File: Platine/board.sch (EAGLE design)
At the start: 10 parts, among them T1 BC847, T2 BC847

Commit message: Update PCB
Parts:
- removed C1, C2: 100µ, resistor:C-EUC0805
- added C4, C5: 100µ, resistor:CPOL-EU153CLV-0605
- added J1: (no value), con-jack:JACK-PLUG1
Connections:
- net +5V: now also J1.3
- net GND: now also J1.1, J1.2
- net N$6: now also C4.-; no longer C1.2
- net N$7: now also C5.-; no longer C2.1
- net N$8: now also C4.+; no longer C1.1
- net N$9: now also C5.+; no longer C2.2
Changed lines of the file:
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@@
 <part name="LED1" library="led" library_urn="urn:adsk.eagle:library:259" deviceset="LED" device="CHIPLED_0805" package3d_urn="urn:adsk.eagle:package:15821/2" value="grün"/>
 <part name="R1" library="resistor" library_urn="urn:adsk.eagle:library:348" deviceset="R-EU_" device="R0805" package3d_urn="urn:adsk.eagle:package:23553/2" value="470"/>
-<part name="C1" library="resistor" library_urn="urn:adsk.eagle:library:348" deviceset="C-EU" device="C0805" package3d_urn="urn:adsk.eagle:package:23617/2" value="100µ"/>
 <part name="LED2" library="led" library_urn="urn:adsk.eagle:library:259" deviceset="LED" device="CHIPLED_0805" package3d_urn="urn:adsk.eagle:package:15821/2" value="grün"/>
 <part name="R2" library="resistor" library_urn="urn:adsk.eagle:library:348" deviceset="R-EU_" device="R0805" package3d_urn="urn:adsk.eagle:package:23553/2" value="470"/>
 <part name="R3" library="resistor" library_urn="urn:adsk.eagle:library:348" deviceset="R-EU_" device="R0805" package3d_urn="urn:adsk.eagle:package:23553/2" value="470"/>
 <part name="R4" library="resistor" library_urn="urn:adsk.eagle:library:348" deviceset="R-EU_" device="R0805" package3d_urn="urn:adsk.eagle:package:23553/2" value="470"/>
-<part name="C2" library="resistor" library_urn="urn:adsk.eagle:library:348" deviceset="C-EU" device="C0805" package3d_urn="urn:adsk.eagle:package:23617/2" value="100µ"/>
 <part name="T1" library="transistor" library_urn="urn:adsk.eagle:library:402" deviceset="BC847" device="" package3d_urn="urn:adsk.eagle:package:28738/2"/>
 <part name="T2" library="transistor" library_urn="urn:adsk.eagle:library:402" deviceset="BC847" device="" package3d_urn="urn:adsk.eagle:package:28738/2"/>
 <part name="P+1" library="supply1" library_urn="urn:adsk.eagle:library:371" deviceset="+5V" device=""/>
 <part name="GND1" library="supply1" library_urn="urn:adsk.eagle:library:371" deviceset="GND" device=""/>
+<part name="J1" library="con-jack" library_urn="urn:adsk.eagle:library:154" deviceset="JACK-PLUG" device="1" package3d_urn="urn:adsk.eagle:package:7494/1"/>
+<part name="P+2" library="supply1" library_urn="urn:adsk.eagle:library:371" deviceset="+5V" device=""/>
+<part name="GND2" library="supply1" library_urn="urn:adsk.eagle:library:371" deviceset="GND" device=""/>
+<part name="C4" library="resistor" library_urn="urn:adsk.eagle:library:348" deviceset="CPOL-EU" device="153CLV-0605" package3d_urn="urn:adsk.eagle:package:23398/2" value="100µ"/>
+<part name="C5" library="resistor" library_urn="urn:adsk.eagle:library:348" deviceset="CPOL-EU" device="153CLV-0605" package3d_urn="urn:adsk.eagle:package:23398/2" value="100µ"/>
 </parts>
 <sheets>
@@
 <attribute name="NAME" x="13.7414" y="46.99" size="1.778" layer="95" rot="R90"/>
 <attribute name="VALUE" x="18.542" y="46.99" size="1.778" layer="96" rot="R90"/>
-</instance>
-<instance part="C1" gate="G$1" x="35.56" y="45.72" smashed="yes" rot="R270">
-<attribute name="NAME" x="35.941" y="44.196" size="1.778" layer="95" rot="R270"/>
-<attribute name="VALUE" x="30.861" y="44.196" size="1.778" layer="96" rot="R270"/>
 </instance>
 <instance part="LED2" gate="G$1" x="15.24" y="63.5" smashed="yes">
@@
 <attribute name="VALUE" x="49.022" y="46.99" size="1.778" layer="96" rot="R90"/>
 </instance>
-<instance part="C2" gate="G$1" x="35.56" y="38.1" smashed="yes" rot="R270">
-<attribute name="NAME" x="35.941" y="36.576" size="1.778" layer="95" rot="R270"/>
-<attribute name="VALUE" x="30.861" y="36.576" size="1.778" layer="96" rot="R270"/>
-</instance>
 <instance part="T1" gate="G$1" x="17.78" y="33.02" smashed="yes" rot="MR0">
 <attribute name="NAME" x="27.94" y="40.64" size="1.778" layer="95" rot="MR0"/>
@@
 <instance part="GND1" gate="1" x="2.54" y="25.4" smashed="yes">
 <attribute name="VALUE" x="0" y="22.86" size="1.778" layer="96"/>
+</instance>
+<instance part="J1" gate="G$1" x="83.82" y="48.26" smashed="yes">
+<attribute name="NAME" x="76.2" y="53.34" size="1.778" layer="95"/>
+<attribute name="VALUE" x="76.2" y="43.18" size="1.778" layer="96"/>
+</instance>
+<instance part="P+2" gate="1" x="93.98" y="58.42" smashed="yes">
+<attribute name="VALUE" x="91.44" y="53.34" size="1.778" layer="96" rot="R90"/>
+</instance>
+<instance part="GND2" gate="1" x="93.98" y="43.18" smashed="yes">
+<attribute name="VALUE" x="91.44" y="40.64" size="1.778" layer="96"/>
+</instance>
+<instance part="C4" gate="G$1" x="35.56" y="45.72" smashed="yes" rot="R270">
+<attribute name="NAME" x="36.0426" y="44.577" size="1.778" layer="95" rot="R270"/>
+<attribute name="VALUE" x="30.9626" y="44.577" size="1.778" layer="96" rot="R270"/>
+</instance>
+<instance part="C5" gate="G$1" x="33.02" y="38.1" smashed="yes" rot="R90">
+<attribute name="NAME" x="32.5374" y="31.623" size="1.778" layer="95" rot="R90"/>
+<attribute name="VALUE" x="37.6174" y="31.623" size="1.778" layer="96" rot="R90"/>
 </instance>
 </instances>
@@
 <junction x="45.72" y="66.04"/>
 </segment>
+<segment>
+<pinref part="J1" gate="G$1" pin="3"/>
+<pinref part="P+2" gate="1" pin="+5V"/>
+<wire x1="88.9" y1="50.8" x2="93.98" y2="50.8" width="0.1524" layer="91"/>
+<wire x1="93.98" y1="50.8" x2="93.98" y2="55.88" width="0.1524" layer="91"/>
+</segment>
 </net>
 <net name="GND" class="0">
@@
 <wire x1="15.24" y1="27.94" x2="53.34" y2="27.94" width="0.1524" layer="91"/>
 </segment>
+<segment>
+<pinref part="J1" gate="G$1" pin="2"/>
+<pinref part="J1" gate="G$1" pin="1"/>
+<wire x1="88.9" y1="48.26" x2="88.9" y2="45.72" width="0.1524" layer="91"/>
+<pinref part="GND2" gate="1" pin="GND"/>
+<wire x1="88.9" y1="45.72" x2="93.98" y2="45.72" width="0.1524" layer="91"/>
+<junction x="88.9" y="45.72"/>
+</segment>
 </net>
 <net name="N$6" class="0">
@@
 <wire x1="15.24" y1="43.18" x2="15.24" y2="45.72" width="0.1524" layer="91"/>
 <wire x1="15.24" y1="43.18" x2="30.48" y2="43.18" width="0.1524" layer="91"/>
-<pinref part="C1" gate="G$1" pin="2"/>
 <wire x1="30.48" y1="43.18" x2="30.48" y2="45.72" width="0.1524" layer="91"/>
 <junction x="15.24" y="43.18"/>
+<pinref part="C4" gate="G$1" pin="-"/>
 </segment>
 </net>
@@
 <pinref part="T2" gate="G$1" pin="C"/>
 <wire x1="53.34" y1="45.72" x2="53.34" y2="38.1" width="0.1524" layer="91"/>
-<pinref part="C2" gate="G$1" pin="1"/>
 <wire x1="38.1" y1="38.1" x2="53.34" y2="38.1" width="0.1524" layer="91"/>
 <junction x="53.34" y="38.1"/>
+<pinref part="C5" gate="G$1" pin="-"/>
 </segment>
 </net>
 <net name="N$8" class="0">
 <segment>
-<pinref part="C1" gate="G$1" pin="1"/>
 <pinref part="R4" gate="G$1" pin="1"/>
 <wire x1="38.1" y1="45.72" x2="45.72" y2="45.72" width="0.1524" layer="91"/>
@@
 <wire x1="45.72" y1="33.02" x2="48.26" y2="33.02" width="0.1524" layer="91"/>
 <junction x="45.72" y="45.72"/>
+<pinref part="C4" gate="G$1" pin="+"/>
 </segment>
 </net>
@@
 <wire x1="22.86" y1="38.1" x2="22.86" y2="33.02" width="0.1524" layer="91"/>
 <wire x1="22.86" y1="33.02" x2="20.32" y2="33.02" width="0.1524" layer="91"/>
-<pinref part="C2" gate="G$1" pin="2"/>
 <wire x1="22.86" y1="38.1" x2="30.48" y2="38.1" width="0.1524" layer="91"/>
 <junction x="22.86" y="38.1"/>
+<pinref part="C5" gate="G$1" pin="+"/>
 </segment>
 </net>

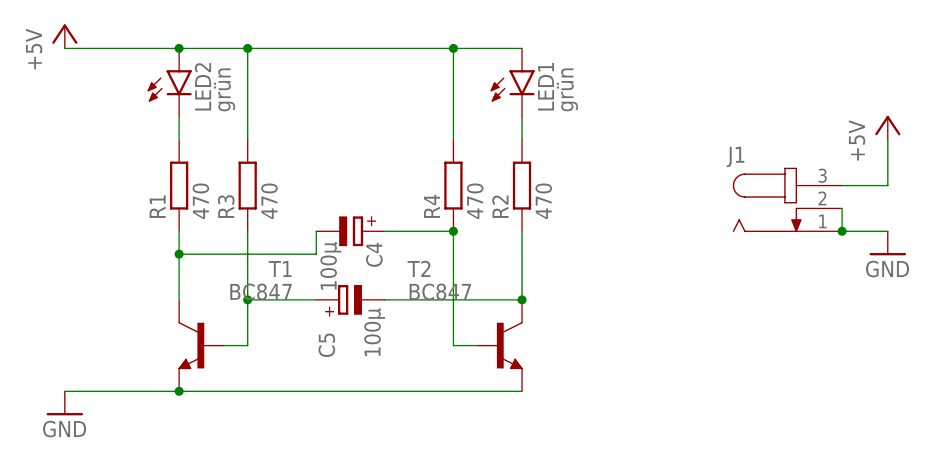
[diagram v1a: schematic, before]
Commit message: Update Platine: SMD Hohlstecker + Wire vergessen
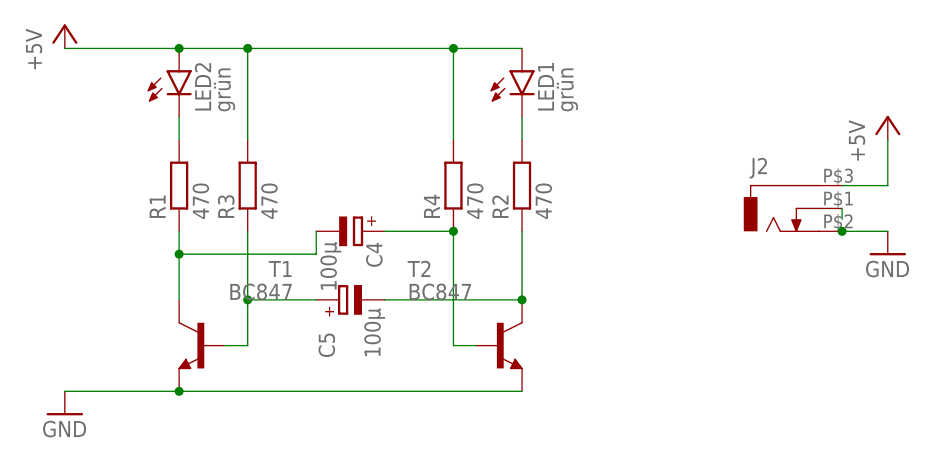
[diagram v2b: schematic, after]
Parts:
- removed J1: (no value), con-jack:JACK-PLUG1
- added J2: (no value), Hohlstecker-SMD:RASM7X2
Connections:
- new net N$19: J2.2
- net +5V: now also J2.1; no longer J1.3
- net GND: now also J2.3; no longer J1.1, J1.2
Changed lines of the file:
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@@
 <part name="P+1" library="supply1" library_urn="urn:adsk.eagle:library:371" deviceset="+5V" device=""/>
 <part name="GND1" library="supply1" library_urn="urn:adsk.eagle:library:371" deviceset="GND" device=""/>
-<part name="J1" library="con-jack" library_urn="urn:adsk.eagle:library:154" deviceset="JACK-PLUG" device="1" package3d_urn="urn:adsk.eagle:package:7494/1"/>
 <part name="P+2" library="supply1" library_urn="urn:adsk.eagle:library:371" deviceset="+5V" device=""/>
 <part name="GND2" library="supply1" library_urn="urn:adsk.eagle:library:371" deviceset="GND" device=""/>
 <part name="C4" library="resistor" library_urn="urn:adsk.eagle:library:348" deviceset="CPOL-EU" device="153CLV-0605" package3d_urn="urn:adsk.eagle:package:23398/2" value="100µ"/>
 <part name="C5" library="resistor" library_urn="urn:adsk.eagle:library:348" deviceset="CPOL-EU" device="153CLV-0605" package3d_urn="urn:adsk.eagle:package:23398/2" value="100µ"/>
+<part name="J2" library="Hohlstecker-SMD" deviceset="RASM7X2" device=""/>
 </parts>
 <sheets>
@@
 <attribute name="VALUE" x="0" y="22.86" size="1.778" layer="96"/>
 </instance>
-<instance part="J1" gate="G$1" x="83.82" y="48.26" smashed="yes">
-<attribute name="NAME" x="76.2" y="53.34" size="1.778" layer="95"/>
-<attribute name="VALUE" x="76.2" y="43.18" size="1.778" layer="96"/>
-</instance>
 <instance part="P+2" gate="1" x="93.98" y="58.42" smashed="yes">
 <attribute name="VALUE" x="91.44" y="53.34" size="1.778" layer="96" rot="R90"/>
@@
 <attribute name="NAME" x="32.5374" y="31.623" size="1.778" layer="95" rot="R90"/>
 <attribute name="VALUE" x="37.6174" y="31.623" size="1.778" layer="96" rot="R90"/>
+</instance>
+<instance part="J2" gate="G$1" x="81.28" y="48.26" smashed="yes">
+<attribute name="NAME" x="78.74" y="52.07" size="1.778" layer="95"/>
+<attribute name="VALUE" x="78.74" y="41.91" size="1.778" layer="96"/>
 </instance>
 </instances>
@@
 </segment>
 <segment>
-<pinref part="J1" gate="G$1" pin="3"/>
 <pinref part="P+2" gate="1" pin="+5V"/>
 <wire x1="88.9" y1="50.8" x2="93.98" y2="50.8" width="0.1524" layer="91"/>
 <wire x1="93.98" y1="50.8" x2="93.98" y2="55.88" width="0.1524" layer="91"/>
+<pinref part="J2" gate="G$1" pin="1"/>
 </segment>
 </net>
@@
 </segment>
 <segment>
-<pinref part="J1" gate="G$1" pin="2"/>
-<pinref part="J1" gate="G$1" pin="1"/>
-<wire x1="88.9" y1="48.26" x2="88.9" y2="45.72" width="0.1524" layer="91"/>
 <pinref part="GND2" gate="1" pin="GND"/>
 <wire x1="88.9" y1="45.72" x2="93.98" y2="45.72" width="0.1524" layer="91"/>
+<wire x1="88.9" y1="45.72" x2="88.9" y2="45.72" width="0.1524" layer="91"/>
+<pinref part="J2" gate="G$1" pin="3"/>
 <junction x="88.9" y="45.72"/>
 </segment>
@@
 </segment>
 </net>
+<net name="N$19" class="0">
+<segment>
+<wire x1="88.9" y1="48.26" x2="88.9" y2="47.0662" width="0.1524" layer="91"/>
+<pinref part="J2" gate="G$1" pin="2"/>
+</segment>
+</net>

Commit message: no text, leave the commit message out
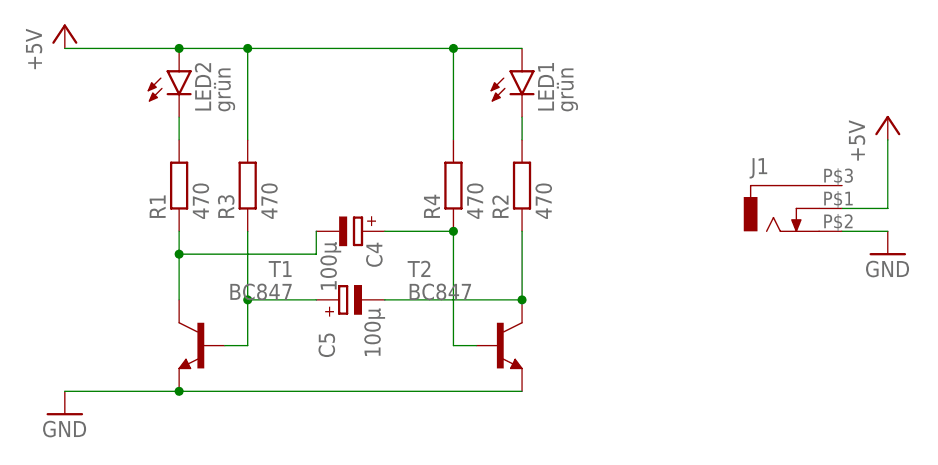
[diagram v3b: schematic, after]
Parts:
- renumbered J2 to J1
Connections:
- removed net N$19: J1.2
- net +5V: now also J1.2; no longer J1.1
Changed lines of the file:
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@@
 <grid distance="0.1" unitdist="inch" unit="inch" style="lines" multiple="1" display="no" altdistance="0.01" altunitdist="inch" altunit="inch"/>
 <layers>
-<layer number="1" name="Top" color="4" fill="1" visible="no" active="no"/>
-<layer number="2" name="Route2" color="1" fill="3" visible="no" active="no"/>
-<layer number="3" name="Route3" color="4" fill="3" visible="no" active="no"/>
-<layer number="4" name="Route4" color="1" fill="4" visible="no" active="no"/>
-<layer number="5" name="Route5" color="4" fill="4" visible="no" active="no"/>
-<layer number="6" name="Route6" color="1" fill="8" visible="no" active="no"/>
-<layer number="7" name="Route7" color="4" fill="8" visible="no" active="no"/>
-<layer number="8" name="Route8" color="1" fill="2" visible="no" active="no"/>
-<layer number="9" name="Route9" color="4" fill="2" visible="no" active="no"/>
-<layer number="10" name="Route10" color="1" fill="7" visible="no" active="no"/>
-<layer number="11" name="Route11" color="4" fill="7" visible="no" active="no"/>
-<layer number="12" name="Route12" color="1" fill="5" visible="no" active="no"/>
-<layer number="13" name="Route13" color="4" fill="5" visible="no" active="no"/>
-<layer number="14" name="Route14" color="1" fill="6" visible="no" active="no"/>
-<layer number="15" name="Route15" color="4" fill="6" visible="no" active="no"/>
-<layer number="16" name="Bottom" color="1" fill="1" visible="no" active="no"/>
-<layer number="17" name="Pads" color="2" fill="1" visible="no" active="no"/>
-<layer number="18" name="Vias" color="2" fill="1" visible="no" active="no"/>
-<layer number="19" name="Unrouted" color="6" fill="1" visible="no" active="no"/>
-<layer number="20" name="Dimension" color="15" fill="1" visible="no" active="no"/>
-<layer number="21" name="tPlace" color="7" fill="9" visible="no" active="no"/>
-<layer number="22" name="bPlace" color="7" fill="1" visible="no" active="no"/>
-<layer number="23" name="tOrigins" color="7" fill="1" visible="no" active="no"/>
-<layer number="24" name="bOrigins" color="15" fill="1" visible="no" active="no"/>
-<layer number="25" name="tNames" color="7" fill="1" visible="no" active="no"/>
-<layer number="26" name="bNames" color="7" fill="1" visible="no" active="no"/>
-<layer number="27" name="tValues" color="7" fill="1" visible="no" active="no"/>
-<layer number="28" name="bValues" color="7" fill="1" visible="no" active="no"/>
+<layer number="1" name="Top" color="4" fill="1" visible="yes" active="no"/>
+<layer number="2" name="Route2" color="16" fill="1" visible="yes" active="no"/>
+<layer number="3" name="Route3" color="17" fill="1" visible="yes" active="no"/>
+<layer number="4" name="Route4" color="18" fill="1" visible="yes" active="no"/>
+<layer number="5" name="Route5" color="19" fill="1" visible="yes" active="no"/>
+<layer number="6" name="Route6" color="25" fill="1" visible="yes" active="no"/>
+<layer number="7" name="Route7" color="26" fill="1" visible="yes" active="no"/>
+<layer number="8" name="Route8" color="27" fill="1" visible="yes" active="no"/>
+<layer number="9" name="Route9" color="28" fill="1" visible="yes" active="no"/>
+<layer number="10" name="Route10" color="29" fill="1" visible="yes" active="no"/>
+<layer number="11" name="Route11" color="30" fill="1" visible="yes" active="no"/>
+<layer number="12" name="Route12" color="20" fill="1" visible="yes" active="no"/>
+<layer number="13" name="Route13" color="21" fill="1" visible="yes" active="no"/>
+<layer number="14" name="Route14" color="22" fill="1" visible="yes" active="no"/>
+<layer number="15" name="Route15" color="23" fill="1" visible="yes" active="no"/>
+<layer number="16" name="Bottom" color="1" fill="1" visible="yes" active="no"/>
+<layer number="17" name="Pads" color="2" fill="1" visible="yes" active="no"/>
+<layer number="18" name="Vias" color="2" fill="1" visible="yes" active="no"/>
+<layer number="19" name="Unrouted" color="6" fill="1" visible="yes" active="no"/>
+<layer number="20" name="Dimension" color="24" fill="1" visible="yes" active="no"/>
+<layer number="21" name="tPlace" color="7" fill="1" visible="yes" active="no"/>
+<layer number="22" name="bPlace" color="7" fill="1" visible="yes" active="no"/>
+<layer number="23" name="tOrigins" color="15" fill="1" visible="yes" active="no"/>
+<layer number="24" name="bOrigins" color="15" fill="1" visible="yes" active="no"/>
+<layer number="25" name="tNames" color="7" fill="1" visible="yes" active="no"/>
+<layer number="26" name="bNames" color="7" fill="1" visible="yes" active="no"/>
+<layer number="27" name="tValues" color="7" fill="1" visible="yes" active="no"/>
+<layer number="28" name="bValues" color="7" fill="1" visible="yes" active="no"/>
 <layer number="29" name="tStop" color="7" fill="3" visible="no" active="no"/>
 <layer number="30" name="bStop" color="7" fill="6" visible="no" active="no"/>
@@
 <layer number="35" name="tGlue" color="7" fill="4" visible="no" active="no"/>
 <layer number="36" name="bGlue" color="7" fill="5" visible="no" active="no"/>
-<layer number="37" name="tTest" color="7" fill="1" visible="no" active="no"/>
-<layer number="38" name="bTest" color="7" fill="1" visible="no" active="no"/>
+<layer number="37" name="tTest" color="7" fill="1" visible="yes" active="no"/>
+<layer number="38" name="bTest" color="7" fill="1" visible="yes" active="no"/>
 <layer number="39" name="tKeepout" color="4" fill="11" visible="no" active="no"/>
 <layer number="40" name="bKeepout" color="1" fill="11" visible="no" active="no"/>
@@
 <layer number="44" name="Drills" color="7" fill="1" visible="no" active="no"/>
 <layer number="45" name="Holes" color="7" fill="1" visible="no" active="no"/>
-<layer number="46" name="Milling" color="3" fill="1" visible="no" active="no"/>
-<layer number="47" name="Measures" color="5" fill="1" visible="no" active="no"/>
-<layer number="48" name="Document" color="7" fill="1" visible="no" active="no"/>
-<layer number="49" name="Reference" color="7" fill="1" visible="no" active="no"/>
-<layer number="51" name="tDocu" color="6" fill="9" visible="no" active="no"/>
-<layer number="52" name="bDocu" color="7" fill="1" visible="no" active="no"/>
+<layer number="46" name="Milling" color="3" fill="1" visible="yes" active="no"/>
+<layer number="47" name="Measures" color="7" fill="1" visible="yes" active="no"/>
+<layer number="48" name="Document" color="7" fill="1" visible="yes" active="no"/>
+<layer number="49" name="Reference" color="7" fill="1" visible="yes" active="no"/>
+<layer number="51" name="tDocu" color="7" fill="1" visible="yes" active="no"/>
+<layer number="52" name="bDocu" color="7" fill="1" visible="yes" active="no"/>
 <layer number="88" name="SimResults" color="9" fill="1" visible="yes" active="yes"/>
 <layer number="89" name="SimProbes" color="9" fill="1" visible="yes" active="yes"/>
@@
 <part name="C4" library="resistor" library_urn="urn:adsk.eagle:library:348" deviceset="CPOL-EU" device="153CLV-0605" package3d_urn="urn:adsk.eagle:package:23398/2" value="100µ"/>
 <part name="C5" library="resistor" library_urn="urn:adsk.eagle:library:348" deviceset="CPOL-EU" device="153CLV-0605" package3d_urn="urn:adsk.eagle:package:23398/2" value="100µ"/>
-<part name="J2" library="Hohlstecker-SMD" deviceset="RASM7X2" device=""/>
+<part name="J1" library="Hohlstecker-SMD" deviceset="RASM7X2" device=""/>
 </parts>
 <sheets>
@@
 <attribute name="VALUE" x="37.6174" y="31.623" size="1.778" layer="96" rot="R90"/>
 </instance>
-<instance part="J2" gate="G$1" x="81.28" y="48.26" smashed="yes">
+<instance part="J1" gate="G$1" x="81.28" y="48.26" smashed="yes">
 <attribute name="NAME" x="78.74" y="52.07" size="1.778" layer="95"/>
 <attribute name="VALUE" x="78.74" y="41.91" size="1.778" layer="96"/>
@@
 <segment>
 <pinref part="P+2" gate="1" pin="+5V"/>
-<wire x1="88.9" y1="50.8" x2="93.98" y2="50.8" width="0.1524" layer="91"/>
-<wire x1="93.98" y1="50.8" x2="93.98" y2="55.88" width="0.1524" layer="91"/>
-<pinref part="J2" gate="G$1" pin="1"/>
+<wire x1="93.98" y1="48.26" x2="93.98" y2="55.88" width="0.1524" layer="91"/>
+<pinref part="J1" gate="G$1" pin="2"/>
+<wire x1="88.9" y1="48.26" x2="93.98" y2="48.26" width="0.1524" layer="91"/>
 </segment>
 </net>
@@
 </segment>
 <segment>
+<pinref part="J1" gate="G$1" pin="3"/>
 <pinref part="GND2" gate="1" pin="GND"/>
 <wire x1="88.9" y1="45.72" x2="93.98" y2="45.72" width="0.1524" layer="91"/>
-<wire x1="88.9" y1="45.72" x2="88.9" y2="45.72" width="0.1524" layer="91"/>
-<pinref part="J2" gate="G$1" pin="3"/>
-<junction x="88.9" y="45.72"/>
 </segment>
 </net>
@@
 </segment>
 </net>
-<net name="N$19" class="0">
-<segment>
-<wire x1="88.9" y1="48.26" x2="88.9" y2="47.0662" width="0.1524" layer="91"/>
-<pinref part="J2" gate="G$1" pin="2"/>
-</segment>
-</net>
